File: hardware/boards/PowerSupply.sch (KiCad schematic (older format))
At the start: 71 parts, among them Q1 Q_NMOS_GSD, Q2 Q_NMOS_GSD, Q3 Q_NMOS_GSD, Q4 Q_NMOS_GSD, Q5 SI7232DN-T1-GE3, U2 ADP5050ACPZ-R7

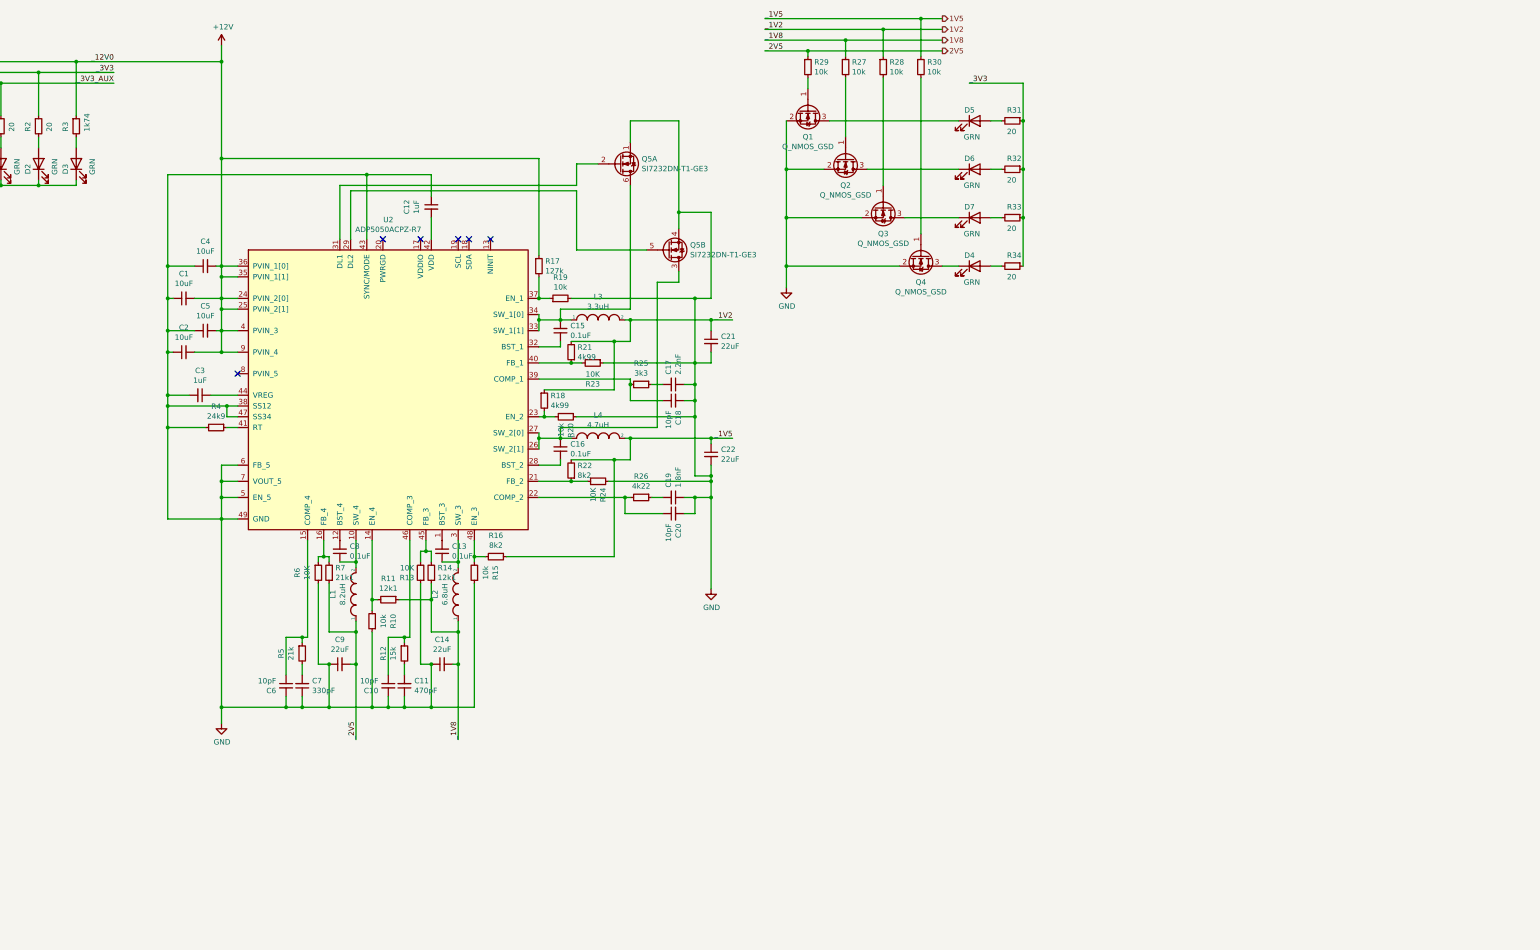
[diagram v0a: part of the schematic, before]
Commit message: Upped the schematic frame size from A4 to A3 to allow for some more breathing room, it was getting stuff in the powersupply schematic
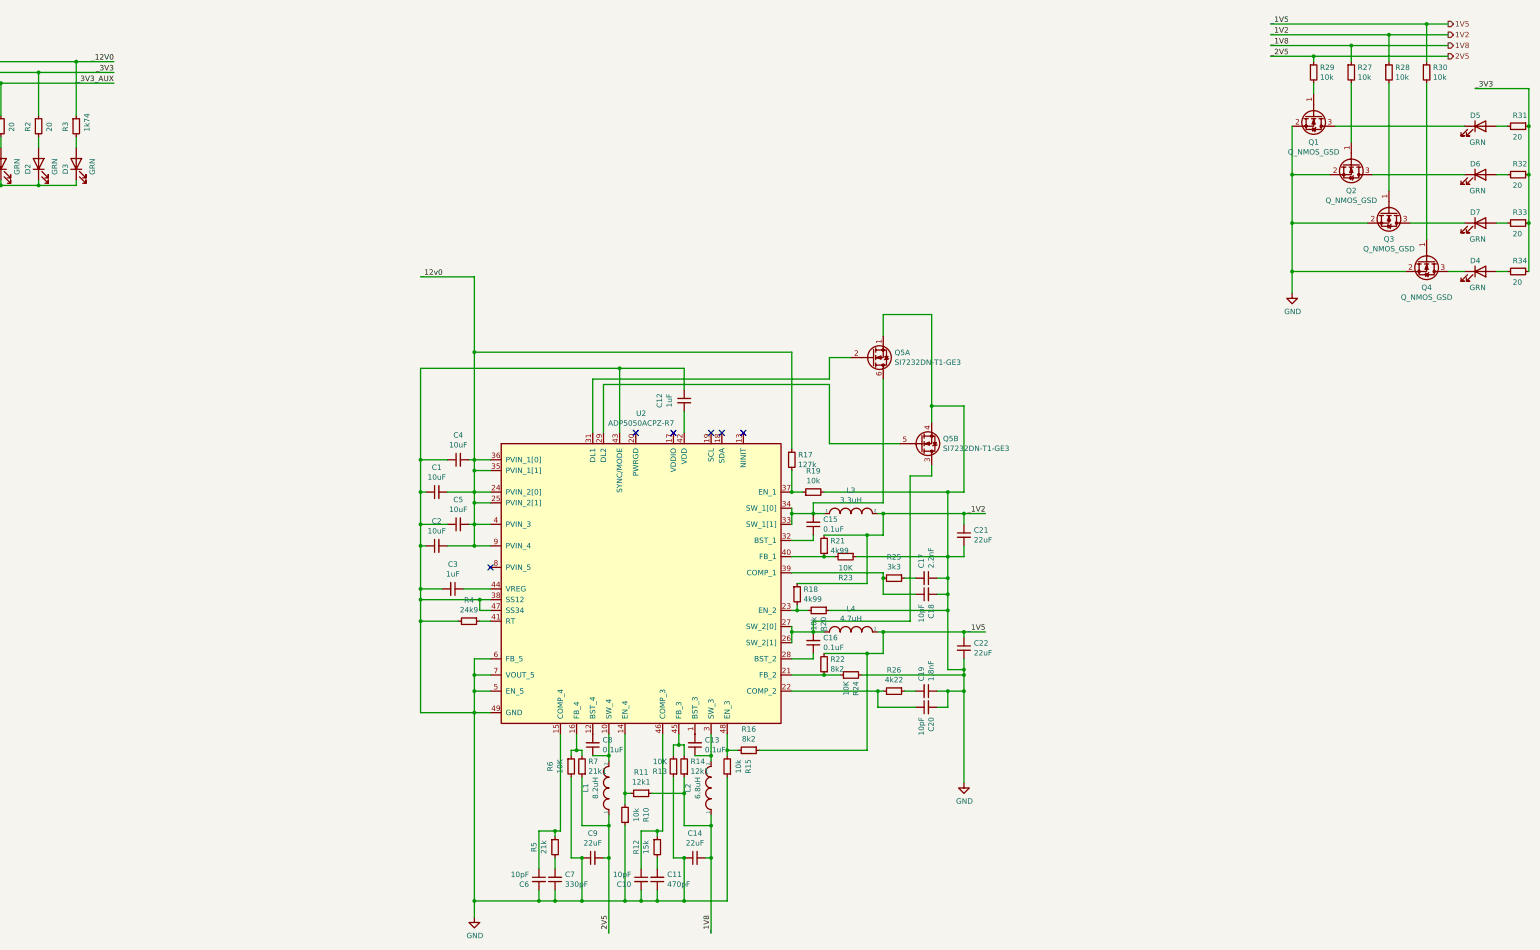
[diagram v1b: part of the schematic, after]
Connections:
- net +12V renamed _12v0
- net _12v0: no longer R3.1
- new net 12V0: R3.1
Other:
- moved on the sheet: C1, C10, C11, C12, C13, C14, C15, C16, C17, C18, C19, C2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

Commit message: Updated the schematics and PCB to bring the initial bootup config DIP switch for the FPGA into it and also ensured that the FPGA had VCCIO8 tied to 3v3 for proper config voltages
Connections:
- net _12v0 is gone; now on net 12V0: C1.2, C2.2, C4.2, C5.2, R17.1, U2.24 (PVIN_2[0]), U2.25 (PVIN_2[1]), U2.35 (PVIN_1[1]), U2.36 (PVIN_1[0]), U2.4 (PVIN_3), U2.9 (PVIN_4)
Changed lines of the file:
@@
 $Descr A3 16535 11693
 encoding utf-8
-Sheet 5 11
+Sheet 8 11
 Title "lethallink - Power Supply"
 Date "2020-06-13"
@@
 Connection ~ 6050 3700
 Text Label 5550 3000 0    50   ~ 0
-_12v0
+_12V0
 $EndSCHEMATC

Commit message: Got a fair bit of the initial layout done for the power supply
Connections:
- net at C16.2, L4.1, U2.26 (SW_2[1])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: now also Q5.6 (D); no longer Q5.3 (D)
- net at U2.29 (DL2): now also Q5.2 (G); no longer Q5.5 (G)
- net at U2.31 (DL1): now also Q5.5 (G); no longer Q5.2 (G)
- net at C15.2, L3.1, U2.33 (SW_1[1])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: now also Q5.3 (D); no longer Q5.6 (D)
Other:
- moved on the sheet: Q5A, Q5B
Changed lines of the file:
@@
 L Device:Q_DUAL_NMOS_S1G1D2S2G2D1 Q5
 U 2 1 5EF3AC59
+P 9750 3750
+F 0 "Q5" H 9955 3704 50  0000 L CNN
+F 1 "SI7232DN-T1-GE3" H 9955 3795 50  0000 L CNN
+F 2 "lethalbit:Si7232DN" H 9950 3750 50  0001 C CNN
+F 3 "https://www.vishay.com/docs/68986/si7232dn.pdf" H 9950 3750 50  0001 C CNN
+F 4 "Vishay Siliconix" H 9750 3750 50  0001 C CNN "MFR"
+F 5 "SI7232DN-T1-GE3" H 9750 3750 50  0001 C CNN "MPN"
+	2    9750 3750
+	1    0    0    1
+$EndComp
+$Comp
+L Device:Q_DUAL_NMOS_S1G1D2S2G2D1 Q5
+U 1 1 5EF3BA04
 P 10200 4550
 F 0 "Q5" H 10405 4504 50  0000 L CNN
@@
 F 4 "Vishay Siliconix" H 10200 4550 50  0001 C CNN "MFR"
 F 5 "SI7232DN-T1-GE3" H 10200 4550 50  0001 C CNN "MPN"
-	2    10200 4550
+	1    10200 4550
 	1    0    0    1
 $EndComp
-$Comp
-L Device:Q_DUAL_NMOS_S1G1D2S2G2D1 Q5
-U 1 1 5EF3BA04
-P 9750 3750
-F 0 "Q5" H 9955 3704 50  0000 L CNN
-F 1 "SI7232DN-T1-GE3" H 9955 3795 50  0000 L CNN
-F 2 "lethalbit:Si7232DN" H 9950 3750 50  0001 C CNN
-F 3 "https://www.vishay.com/docs/68986/si7232dn.pdf" H 9950 3750 50  0001 C CNN
-F 4 "Vishay Siliconix" H 9750 3750 50  0001 C CNN "MFR"
-F 5 "SI7232DN-T1-GE3" H 9750 3750 50  0001 C CNN "MPN"
-	1    9750 3750
-	1    0    0    1
-$EndComp

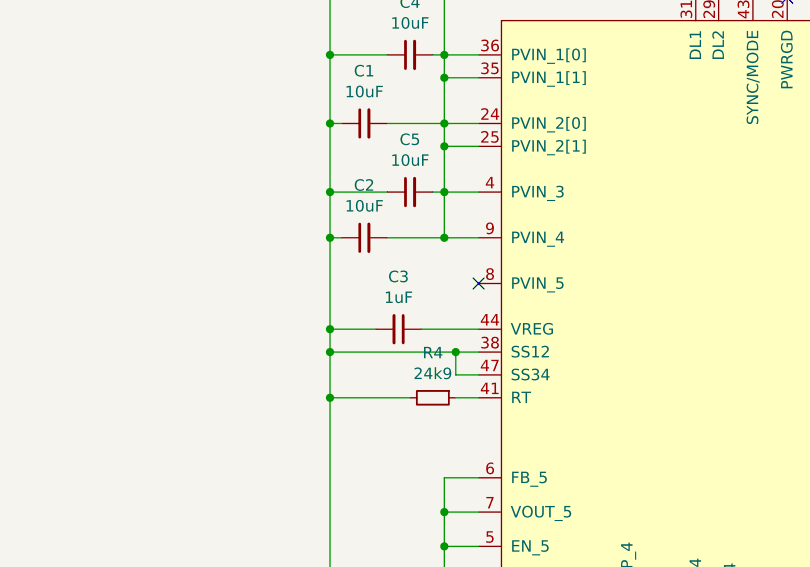
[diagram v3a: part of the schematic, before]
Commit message: Lots more place and routing done for the power supply, only the feeback and enable voltage deviders left to go, along with joining the two halfs with a common +12v pour
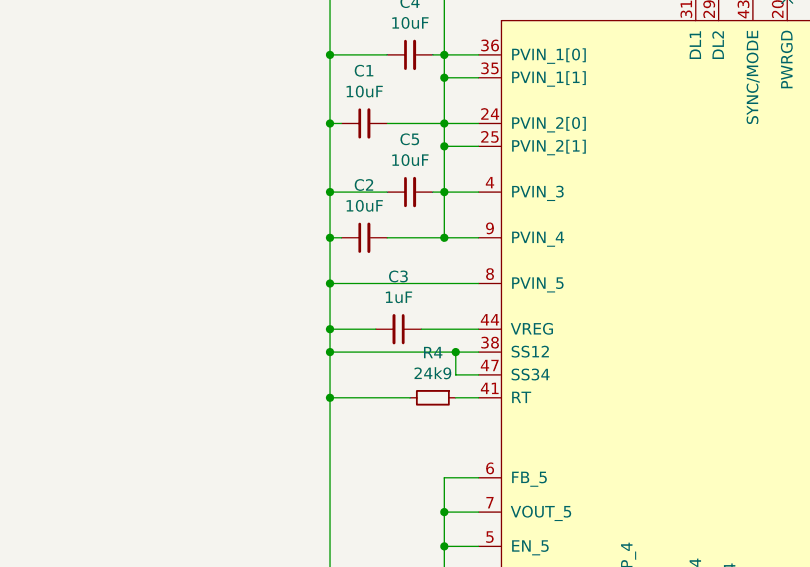
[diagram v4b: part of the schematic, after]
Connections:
- net GND: now also U2.8 (PVIN_5)
- no-connect marks 6 -> 5
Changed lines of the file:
@@
 Connection ~ 5550 5500
 Wire Wire Line
-	5550 5500 5550 5900
+	5550 5500 5550 5700
 Wire Wire Line
 	6050 5100 6050 5300
@@
 	1    0    0    -1
 $EndComp
-NoConn ~ 6200 5700
 Wire Wire Line
 	6050 3700 6050 3000
@@
 Text Label 5550 3000 0    50   ~ 0
 _12V0
+Wire Wire Line
+	6200 5700 5550 5700
+Connection ~ 5550 5700
+Wire Wire Line
+	5550 5700 5550 5900
 $EndSCHEMATC
